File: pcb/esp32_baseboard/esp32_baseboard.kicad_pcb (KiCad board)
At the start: 2 copper layers, 70 x 60 mm, 1 part, among them U1 ESP32_DevKit_V1_30Pin

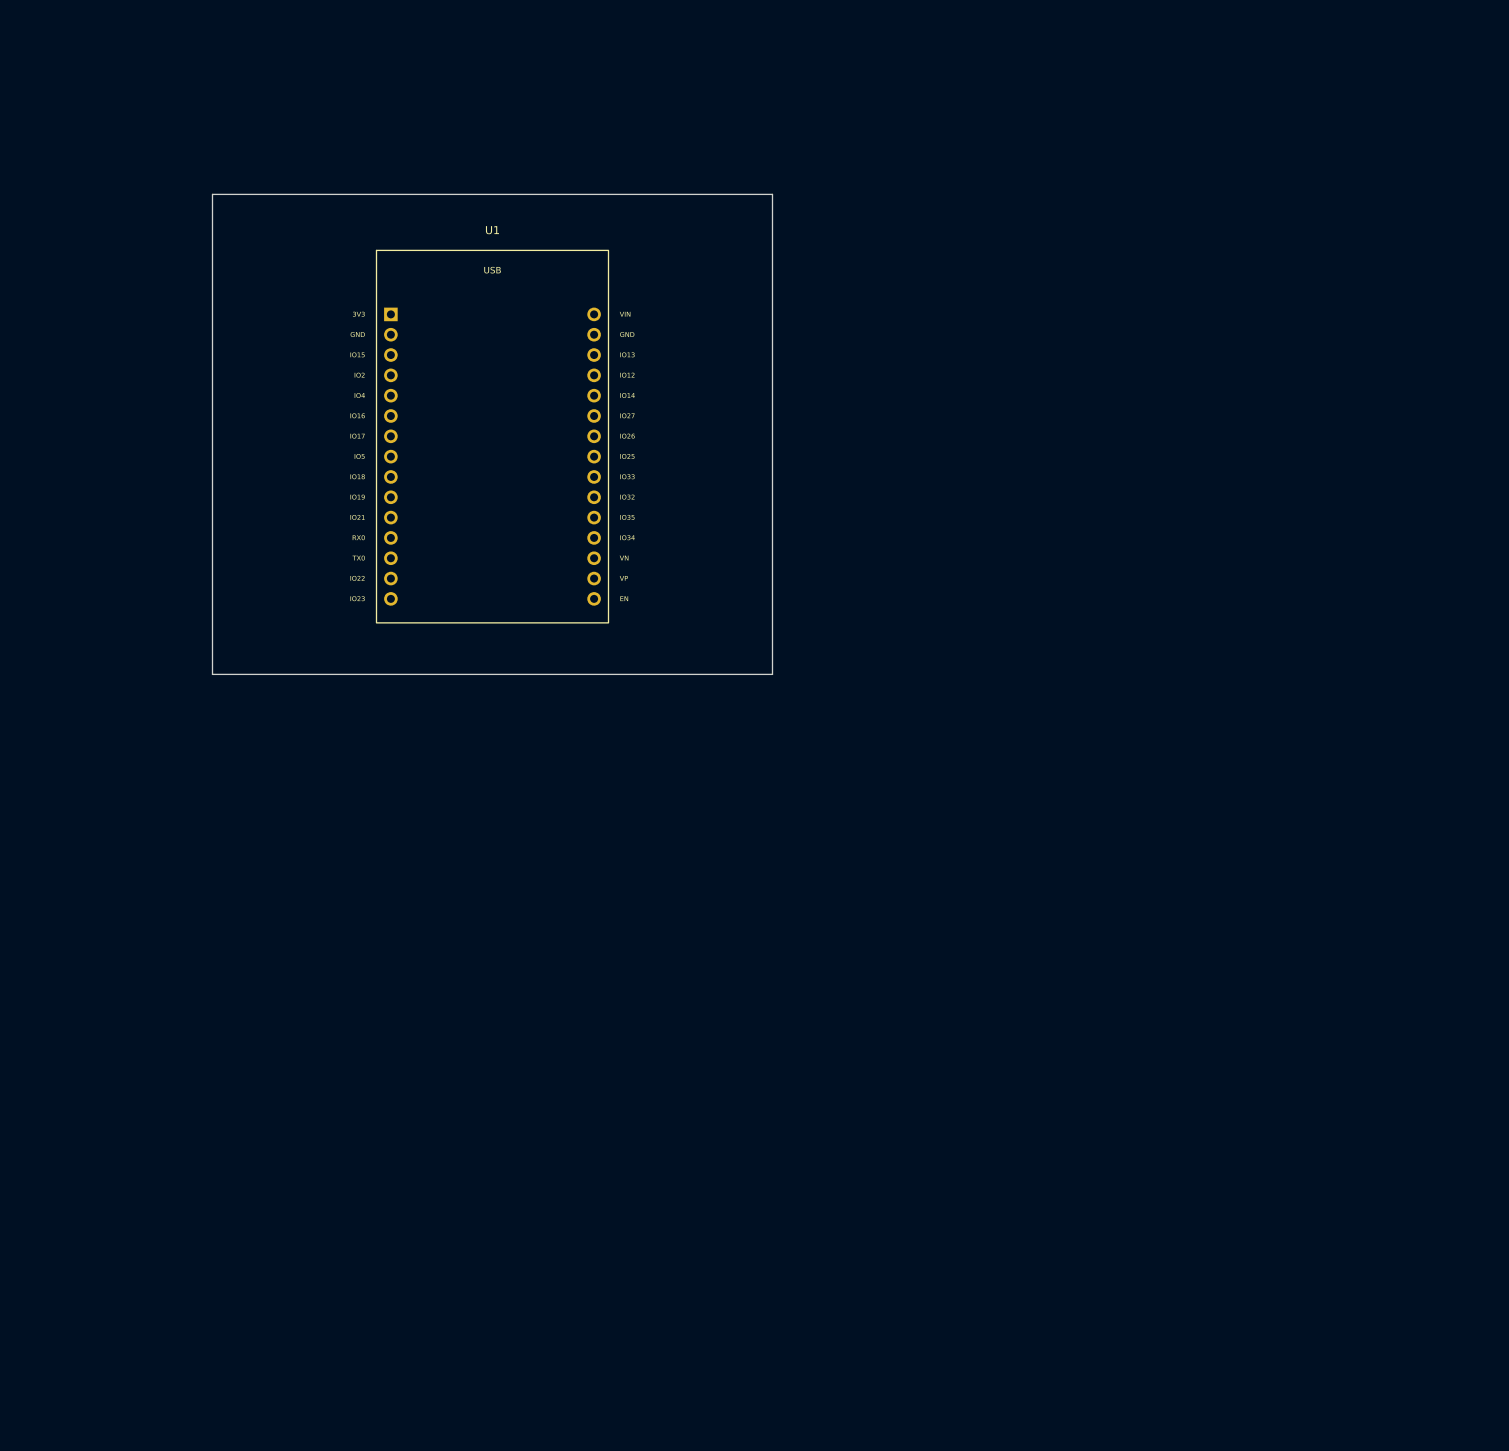
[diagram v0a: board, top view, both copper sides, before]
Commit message: tạo PCB mạch base board ghép nối các sub module
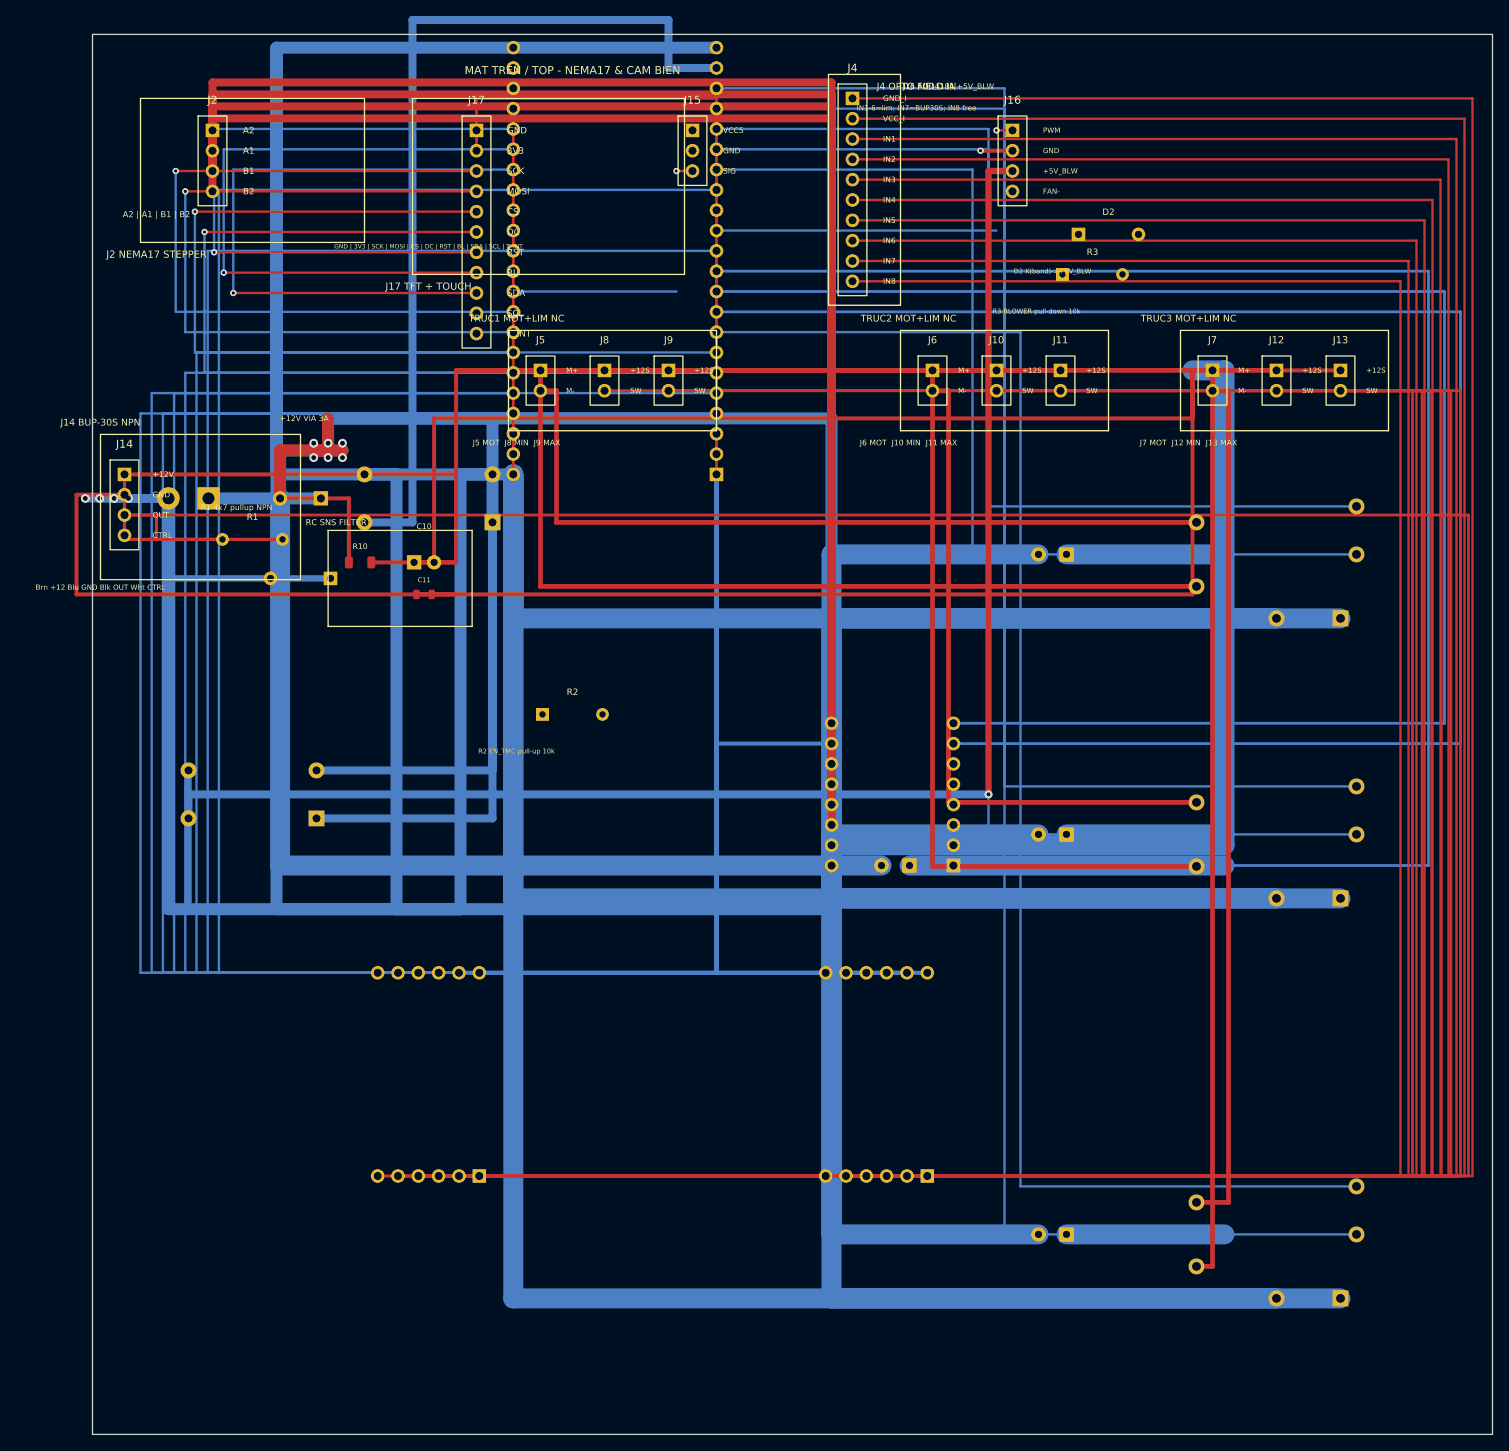
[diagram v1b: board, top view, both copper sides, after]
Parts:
- added C10: 47u/25V, ESP32_Carrier:CP_Radial_D6_47u_25V, F.Cu at (76.5, 96.0)
- added C11: 100n, ESP32_Carrier:C_0805_100n, F.Cu at (76.5, 100.0)
- added C20: 470u/25V, ESP32_Carrier:CP_Radial_D8_470u_25V, B.Cu at (135.4, 133.9)
- added C21: 470u/25V, ESP32_Carrier:CP_Radial_D8_470u_25V, B.Cu at (155.0, 95.0)
- added C22: 470u/25V, ESP32_Carrier:CP_Radial_D8_470u_25V, B.Cu at (155.0, 130.0)
- added C23: 470u/25V, ESP32_Carrier:CP_Radial_D8_470u_25V, B.Cu at (155.0, 180.0)
- added D1: P6KE15A, ESP32_Carrier:Diode_TVS_DO41, B.Cu at (61.0, 98.0)
- added D2: 1N5819, ESP32_Carrier:Diode_TVS_DO41, F.Cu at (162.0, 55.0)
- added F1: PTC_3A_30V, ESP32_Carrier:Fuse_PTC_Radial_5.1mm, B.Cu at (61.0, 88.0)
- added J1: Screw_12V_IN, ESP32_Carrier:TerminalBlock_2P_5.0mm, B.Cu at (47.0, 88.0)
- added J10: LIM_MIN_NC, ESP32_Carrier:PinHeader_1x02_LimitSW, F.Cu at (148.0, 72.0)
- added J11: LIM_MAX_NC, ESP32_Carrier:PinHeader_1x02_LimitSW, F.Cu at (156.0, 72.0)
- added J12: LIM_MIN_NC, ESP32_Carrier:PinHeader_1x02_LimitSW, F.Cu at (183.0, 72.0)
- added J13: LIM_MAX_NC, ESP32_Carrier:PinHeader_1x02_LimitSW, F.Cu at (191.0, 72.0)
- added J14: BUP_30S, ESP32_Carrier:PinHeader_1x04_BUP30S, F.Cu at (39.0, 85.0)
- added J15: BUZZER_5V, ESP32_Carrier:PinHeader_1x03_Buzzer, F.Cu at (110.0, 42.0)
- added J16: AOD4184, ESP32_Carrier:PinHeader_1x04_MOSFET, F.Cu at (150.0, 42.0)
- added J17: TFT_TOUCH, ESP32_Carrier:PinHeader_1x11_TFT, F.Cu at (83.0, 42.0)
- added J2: NEMA17_OUT, ESP32_Carrier:PinHeader_1x04_Motor, F.Cu at (50.0, 42.0)
- added J4: OPTO_FIELD_IN, ESP32_Carrier:PinHeader_1x10_OptoField, F.Cu at (130.0, 38.0)
- added J5: GA12_N20, ESP32_Carrier:PinHeader_1x02_MotorDC, F.Cu at (91.0, 72.0)
- added J6: GA12_N20, ESP32_Carrier:PinHeader_1x02_MotorDC, F.Cu at (140.0, 72.0)
- added J7: GA12_N20, ESP32_Carrier:PinHeader_1x02_MotorDC, F.Cu at (175.0, 72.0)
- added J8: LIM_MIN_NC, ESP32_Carrier:PinHeader_1x02_LimitSW, F.Cu at (99.0, 72.0)
- added J9: LIM_MAX_NC, ESP32_Carrier:PinHeader_1x02_LimitSW, F.Cu at (107.0, 72.0)
- added R1: 4k7, ESP32_Carrier:R_Axial_4k7_BUP, F.Cu at (55.0, 93.1)
- added R10: 10R, ESP32_Carrier:R_1206_10R, F.Cu at (68.5, 96.0)
- added R2: 10k, ESP32_Carrier:R_Axial_4k7_BUP, F.Cu at (95.0, 115.0)
- added R3: 10k, ESP32_Carrier:R_Axial_4k7_BUP, F.Cu at (160.0, 60.0)
- added U2: MP1584_5V3A, ESP32_Carrier:MP1584_5V3A, B.Cu at (77.0, 88.0)
- added U3: TMC2209, ESP32_Carrier:TMC2209_StepStick, B.Cu at (135.0, 125.0)
- added U4: PC817_4CH, ESP32_Carrier:PC817_4CH_Opto, B.Cu at (77.0, 160.0)
- added U5: DRV8871_Module, ESP32_Carrier:DRV8871_Module, B.Cu at (183.0, 95.0)
- added U6: DRV8871_Module, ESP32_Carrier:DRV8871_Module, B.Cu at (183.0, 130.0)
- added U7: DRV8871_Module, ESP32_Carrier:DRV8871_Module, B.Cu at (183.0, 180.0)
- added U8: MP1584_BLW, ESP32_Carrier:MP1584_5V3A, B.Cu at (55.0, 125.0)
- added U9: PC817_4CH, ESP32_Carrier:PC817_4CH_Opto, B.Cu at (133.0, 160.0)
- U1: value ESP32_DevKit_V1_30Pin -> ESP32_S3_DevKitC_1; footprint ESP32_Carrier:ESP32_DevKit_V1_30Pin_Socket -> ESP32_Carrier:ESP32_S3_DevKitC_44Pin_Socket; moved to B.Cu
- moved U1 45.3 mm to (113.0, 85.0), turned to 180 degrees
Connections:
- U1 pad 1: (no net) -> +3V3
- U1 pad 10: (no net) -> /DIR
- U1 pad 11: (no net) -> /EN_TMC
- U1 pad 12: (no net) -> /OPTO_OUT7
- U1 pad 13: (no net) -> /BLOWER
- U1 pad 14: (no net) -> /TFT_RST
- U1 pad 15: (no net) -> /OPTO_OUT8
- U1 pad 16: (no net) -> /DC1_IN1
- U1 pad 17: (no net) -> /DC1_IN2
- U1 pad 18: (no net) -> /DC2_IN1
- U1 pad 19: (no net) -> /DC2_IN2
- U1 pad 2: (no net) -> +3V3
- U1 pad 20: (no net) -> /DC3_IN1
- U1 pad 21: (no net) -> +5V
- U1 pad 22: (no net) -> GND
- U1 pad 23: (no net) -> GND
- U1 pad 26: (no net) -> /OPTO_OUT1
- U1 pad 27: (no net) -> /OPTO_OUT2
- U1 pad 28: (no net) -> /TFT_CS
- U1 pad 29: (no net) -> /TP_INT
- U1 pad 30: (no net) -> /TFT_MOSI
- U1 pad 4: (no net) -> /OPTO_OUT3
- U1 pad 5: (no net) -> /OPTO_OUT4
- U1 pad 6: (no net) -> /OPTO_OUT5
- U1 pad 7: (no net) -> /OPTO_OUT6
- U1 pad 8: (no net) -> /DC3_IN2
- U1 pad 9: (no net) -> /STEP
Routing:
- net GND: track 0.00 -> 2326.1 mm, vias 0 -> 5
- net +12V: track 0.00 -> 866.3 mm, vias 0 -> 6
- net /OPTO_IN1: track 0.00 -> 665.2 mm, vias 0 -> 1
- net /OPTO_IN2: track 0.00 -> 655.4 mm, vias 0 -> 1
- net /OPTO_IN3: track 0.00 -> 612.5 mm, vias 0 -> 1
- net /OPTO_IN7: track 0.00 -> 605.4 mm, vias 0 -> 1
- net /OPTO_IN4: track 0.00 -> 602.7 mm, vias 0 -> 1
- net +12V_SNS: track 0.00 -> 487.6 mm
- net /OPTO_IN5: track 0.00 -> 441.5 mm, vias 0 -> 1
- net /OPTO_IN6: track 0.00 -> 431.6 mm, vias 0 -> 1
- net /OPTO_VCC_I: track 0.00 -> 390.4 mm
- net +3V3: track 0.00 -> 312.2 mm
- net /OPTO_IN8: track 0.00 -> 252.2 mm
- net /OPTO_OUT8: track 0.00 -> 235.9 mm
- net /OPTO_OUT7: track 0.00 -> 233.6 mm
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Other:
- board size 70 x 60 mm -> 175 x 175 mm
- net class Default added: clearance 0.2, trace_width 0.25, via_dia 0.6, via_drill 0.3
- net class Power added: clearance 0.25, trace_width 1.5, via_dia 1.1, via_drill 0.6
- board text added: "+12V VIA 3A"
- board text added: "12V -> 5V logic"
- board text added: "2x PC817 4CH | OUT=MCU IN=J4 field"
- board text added: "A2 | A1 | B1 | B2"
- board text added: "AOD4184 / blower only"
- board text added: "Brn +12 Blu GND Blk OUT Wht CTRL"
- board text added: "C20 470u TMC"
- board text added: "C21 470u U5"
- board text added: "C22 470u U6"
- board text added: "C23 470u U7"
- board text added: "D2 K(band)->+5V_BLW"
- board text added: "F1 PTC + D1 TVS"
- board text added: "GND star gap chi gap tai J1-"
- board text added: "GND | 3V3 | SCK | MOSI | CS | DC | RST | BL | SDA | SCL | T_INT"
- board text added: "IN1-6=lim; IN7=BUP30S; IN8 free"
- board text added: "J1 NGUON 12V-3A"
- board text added: "J14 BUP-30S NPN"
- board text added: "J16 AOD4184 +5V_BLW"
- board text added: "J17 TFT + TOUCH"
- board text added: "J2 NEMA17 STEPPER"
- board text added: "J4 OPTO FIELD IN"
- board text added: "J5 MOT J8 MIN J9 MAX"
- board text added: "J6 MOT J10 MIN J11 MAX"
- board text added: "J7 MOT J12 MIN J13 MAX"
- board text added: "MAT DUOI / BOTTOM - MODULE ROI"
- board text added: "MAT TREN / TOP - NEMA17 & CAM BIEN"
- board text added: "R1 4k7 pullup NPN"
- board text added: "R2 EN_TMC pull-up 10k"
- board text added: "R3 BLOWER pull-down 10k"
- board text added: "RC SNS FILTER"
- board text added: "STAR +12V: MOT 2.5mm | SNS 0.5mm+RC"
- board text added: "TRUC1 MOT+LIM NC"
- board text added: "TRUC2 MOT+LIM NC"
- board text added: "TRUC3 MOT+LIM NC"
- board text added: "U1 ESP32 DevKit V1"
- board text added: "U2 MP1584EN LOGIC 5V"
- board text added: "U3 TMC2209"
- board text added: "U4 PC817 4CH"
- board text added: "U5 DRV8871 GA12"
- board text added: "U6 DRV8871 GA12"
- board text added: "U7 DRV8871 GA12"
- board text added: "U8 MP1584 +5V_BLW"
- board text added: "U9 PC817 4CH"
- board text added: "VM=12V"
- board text added: "stepstick NEMA17"
- board text added: "via farm 6x0.6mm >=3A"

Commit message: sửa lỗi ngắn mạch trên board
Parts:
- removed U8: MP1584_BLW, ESP32_Carrier:MP1584_5V3A
- added H1: M3, ESP32_Carrier:MountingHole_M3, F.Cu at (38.5, 33.5)
- added H2: M3, ESP32_Carrier:MountingHole_M3, F.Cu at (256.5, 33.5)
- added H3: M3, ESP32_Carrier:MountingHole_M3, F.Cu at (38.5, 158.5)
- added H4: M3, ESP32_Carrier:MountingHole_M3, F.Cu at (256.5, 158.5)
- added J18: EC11_ENC, ESP32_Carrier:PinHeader_1x04_ENC, F.Cu at (95.0, 40.0)
- J17: footprint ESP32_Carrier:PinHeader_1x11_TFT -> ESP32_Carrier:PinHeader_1x10_TFT
- moved J14 204.4 mm to (243.0, 72.0)
- moved R1 178.5 mm to (233.0, 80.1)
- moved U3 85.2 mm to (217.0, 102.0)
- moved C20 85.2 mm to (217.4, 110.9)
- moved J4 83.0 mm to (213.0, 38.0)
- moved C23 77.2 mm to (221.0, 140.0)
- moved U7 72.1 mm to (243.0, 140.0)
- moved C22 67.5 mm to (221.0, 116.0)
- moved C21 66.1 mm to (221.0, 92.0)
- moved U6 61.6 mm to (243.0, 116.0)
- moved U5 60.1 mm to (243.0, 92.0)
- moved R2 48.5 mm to (143.0, 108.0)
- moved U1 40.3 mm to (133.0, 120.0)
- moved J5 38.0 mm to (53.0, 72.0)
- moved J8 38.0 mm to (61.0, 72.0)
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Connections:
- net /I2C_SCL renamed /T_CS
- D2 pad 1: +5V_BLW -> +12V
- J16 pad 3: +5V_BLW -> +12V
- J17 pad 5: /TFT_CS -> /TFT_MISO
- J17 pad 6: /TFT_DC -> /TFT_CS
- J17 pad 7: /TFT_RST -> /TFT_DC
- J17 pad 8: /TFT_BL -> /TFT_RST
- J17 pad 9: /I2C_SDA -> /TFT_BL
- U1 pad 15: /OPTO_OUT8 -> /ENC_A
- U1 pad 29: /TP_INT -> /ENC_B
- U1 pad 39: /I2C_SDA -> /TFT_MISO
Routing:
- net GND: track 2326.1 -> 1179.7 mm, vias 5 -> 0
- net +12V: track 866.3 -> 435.4 mm, vias 6 -> 0
- net /OPTO_IN2: track 655.4 -> 253.0 mm, vias 1 -> 0
- net /OPTO_IN1: track 665.2 -> 270.5 mm, vias 1 -> 0
- net /OPTO_IN3: track 612.5 -> 257.1 mm, vias 1 -> 0
- net /OPTO_IN4: track 602.7 -> 255.2 mm, vias 1 -> 0
- net /TFT_MOSI: track 95.0 -> 437.6 mm, vias 1 -> 0
- net /TFT_SCK: track 97.4 -> 423.0 mm, vias 1 -> 0
- net /BLOWER: track 37.0 -> 359.9 mm, vias 1 -> 0
- net /OPTO_IN5: track 441.5 -> 182.9 mm, vias 1 -> 0
- net /OPTO_IN6: track 431.6 -> 192.1 mm, vias 1 -> 0
- net /OPTO_OUT8: track 235.9 -> 0.00 mm
- net +12V_SNS: track 487.6 -> 273.2 mm
- net /MotB1: track 170.2 -> 378.9 mm
- net /OPTO_OUT5: track 229.1 -> 24.9 mm
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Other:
- board size 175 x 175 mm -> 225 x 132 mm
- board text added: "1 POWER J1/U2"
- board text added: "2 MCU U1"
- board text added: "3 TMC"
- board text added: "B STEP"
- board text added: "B.Cu bus"
- board text added: "BOTTOM — 1 POWER | 2 MCU | 3 TMC | 4 OPTO | 5 DRV"
- board text added: "C HMI J17/J18/J15"
- board text added: "D SENSE"
- board text added: "D2 K(band)->+12V"
- board text added: "E+F DC MOT + LIMIT (cap truc)"
- board text added: "G BLW"
- board text added: "GND 3V3 A=IO9 B=IO41"
- board text added: "J16 AOD4184 +12V pump"
- board text added: "J18 ENC wall-mount EC11"
- board text added: "M3x4 corner mount"
- board text added: "TOP 225x132 — giac theo nhom | BOTTOM module"
- board text removed: "12V -> 5V logic"
- board text removed: "A2 | A1 | B1 | B2"
- board text removed: "AOD4184 / blower only"
- board text removed: "D2 K(band)->+5V_BLW"
- board text removed: "GND | 3V3 | SCK | MOSI | CS | DC | RST | BL | SDA | SCL | T_INT"
- board text removed: "J1 NGUON 12V-3A"
- board text removed: "J16 AOD4184 +5V_BLW"
- board text removed: "J17 TFT + TOUCH"
- board text removed: "J2 NEMA17 STEPPER"
- board text removed: "MAT DUOI / BOTTOM - MODULE ROI"
- board text removed: "MAT TREN / TOP - NEMA17 & CAM BIEN"
- board text removed: "U1 ESP32 DevKit V1"
- board text removed: "U2 MP1584EN LOGIC 5V"
- board text removed: "U3 TMC2209"
- board text removed: "U8 MP1584 +5V_BLW"
- board text removed: "stepstick NEMA17"
- board text removed: "via farm 6x0.6mm >=3A"
